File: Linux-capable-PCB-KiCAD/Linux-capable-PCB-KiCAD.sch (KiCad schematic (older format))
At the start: 36 parts, among them U1 A33

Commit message: Assigned footprints to components, antenna and a couple of other footprints need to be assigned
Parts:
- C1, C10, C11, C12, C13, C14, C15, C16, C17, C18, C19, C2, C20, C21, C22, C23, C24, C25, C3, C4, C5, C6, C7, C8, C9: footprint (none) -> Capacitor_SMD:C_0603_1608Metric
- MK1, MK2, MK3, MK4: footprint (none) -> MountingHole:MountingHole_3mm
- R1, R2, R3, R4, R5, R6: footprint (none) -> Resistor_SMD:R_0603_1608Metric
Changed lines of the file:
@@
 F 0 "R1" H 1920 2096 50  0000 L CNN
 F 1 "1k" H 1920 2005 50  0000 L CNN
-F 2 "" V 1780 2050 50  0001 C CNN
+F 2 "Resistor_SMD:R_0603_1608Metric" V 1780 2050 50  0001 C CNN
 F 3 "" H 1850 2050 50  0001 C CNN
 	1    1850 2050
@@
 F 0 "R2" H 1920 2496 50  0000 L CNN
 F 1 "1k" H 1920 2405 50  0000 L CNN
-F 2 "" V 1780 2450 50  0001 C CNN
+F 2 "Resistor_SMD:R_0603_1608Metric" V 1780 2450 50  0001 C CNN
 F 3 "" H 1850 2450 50  0001 C CNN
 	1    1850 2450
@@
 F 0 "C1" H 1515 2096 50  0000 L CNN
 F 1 "100n" H 1515 2005 50  0000 L CNN
-F 2 "" H 1438 1900 50  0001 C CNN
+F 2 "Capacitor_SMD:C_0603_1608Metric" H 1438 1900 50  0001 C CNN
 F 3 "" H 1400 2050 50  0001 C CNN
 	1    1400 2050
@@
 F 0 "C2" H 1515 2496 50  0000 L CNN
 F 1 "100n" H 1515 2405 50  0000 L CNN
-F 2 "" H 1438 2300 50  0001 C CNN
+F 2 "Capacitor_SMD:C_0603_1608Metric" H 1438 2300 50  0001 C CNN
 F 3 "" H 1400 2450 50  0001 C CNN
 	1    1400 2450
@@
 F 0 "C25" H 8565 4396 50  0000 L CNN
 F 1 "100n" H 8565 4305 50  0000 L CNN
-F 2 "" H 8488 4200 50  0001 C CNN
+F 2 "Capacitor_SMD:C_0603_1608Metric" H 8488 4200 50  0001 C CNN
 F 3 "" H 8450 4350 50  0001 C CNN
 	1    8450 4350
@@
 F 0 "R6" V 7093 2450 50  0000 C CNN
 F 1 "0R" V 7184 2450 50  0000 C CNN
-F 2 "" V 7230 2450 50  0001 C CNN
+F 2 "Resistor_SMD:R_0603_1608Metric" V 7230 2450 50  0001 C CNN
 F 3 "" H 7300 2450 50  0001 C CNN
 	1    7300 2450
@@
 F 0 "C17" H 7065 1846 50  0000 L CNN
 F 1 "10u" H 7065 1755 50  0000 L CNN
-F 2 "" H 6988 1650 50  0001 C CNN
+F 2 "Capacitor_SMD:C_0603_1608Metric" H 6988 1650 50  0001 C CNN
 F 3 "" H 6950 1800 50  0001 C CNN
 	1    6950 1800
@@
 F 0 "C22" H 7565 1846 50  0000 L CNN
 F 1 "100n" H 7565 1755 50  0000 L CNN
-F 2 "" H 7488 1650 50  0001 C CNN
+F 2 "Capacitor_SMD:C_0603_1608Metric" H 7488 1650 50  0001 C CNN
 F 3 "" H 7450 1800 50  0001 C CNN
 	1    7450 1800
@@
 F 0 "C13" H 6565 1846 50  0000 L CNN
 F 1 "22u" H 6500 1700 50  0000 L CNN
-F 2 "" H 6488 1650 50  0001 C CNN
+F 2 "Capacitor_SMD:C_0603_1608Metric" H 6488 1650 50  0001 C CNN
 F 3 "" H 6450 1800 50  0001 C CNN
 	1    6450 1800
@@
 F 0 "C9" H 6165 1846 50  0000 L CNN
 F 1 "100n" H 6100 1700 50  0000 L CNN
-F 2 "" H 6088 1650 50  0001 C CNN
+F 2 "Capacitor_SMD:C_0603_1608Metric" H 6088 1650 50  0001 C CNN
 F 3 "" H 6050 1800 50  0001 C CNN
 	1    6050 1800
@@
 F 0 "C5" H 5765 1846 50  0000 L CNN
 F 1 "100n" H 5700 1700 50  0000 L CNN
-F 2 "" H 5688 1650 50  0001 C CNN
+F 2 "Capacitor_SMD:C_0603_1608Metric" H 5688 1650 50  0001 C CNN
 F 3 "" H 5650 1800 50  0001 C CNN
 	1    5650 1800
@@
 F 0 "C3" H 5315 1846 50  0000 L CNN
 F 1 "100n" H 5250 1700 50  0000 L CNN
-F 2 "" H 5238 1650 50  0001 C CNN
+F 2 "Capacitor_SMD:C_0603_1608Metric" H 5238 1650 50  0001 C CNN
 F 3 "" H 5200 1800 50  0001 C CNN
 	1    5200 1800
@@
 F 0 "C6" H 5765 2846 50  0000 L CNN
 F 1 "100n" H 5700 2700 50  0000 L CNN
-F 2 "" H 5688 2650 50  0001 C CNN
+F 2 "Capacitor_SMD:C_0603_1608Metric" H 5688 2650 50  0001 C CNN
 F 3 "" H 5650 2800 50  0001 C CNN
 	1    5650 2800
@@
 F 0 "C10" H 6165 2846 50  0000 L CNN
 F 1 "100n" H 6100 2700 50  0000 L CNN
-F 2 "" H 6088 2650 50  0001 C CNN
+F 2 "Capacitor_SMD:C_0603_1608Metric" H 6088 2650 50  0001 C CNN
 F 3 "" H 6050 2800 50  0001 C CNN
 	1    6050 2800
@@
 F 0 "C14" H 6565 2846 50  0000 L CNN
 F 1 "100n" H 6500 2700 50  0000 L CNN
-F 2 "" H 6488 2650 50  0001 C CNN
+F 2 "Capacitor_SMD:C_0603_1608Metric" H 6488 2650 50  0001 C CNN
 F 3 "" H 6450 2800 50  0001 C CNN
 	1    6450 2800
@@
 F 0 "C7" H 5765 3946 50  0000 L CNN
 F 1 "22u" H 5700 3800 50  0000 L CNN
-F 2 "" H 5688 3750 50  0001 C CNN
+F 2 "Capacitor_SMD:C_0603_1608Metric" H 5688 3750 50  0001 C CNN
 F 3 "" H 5650 3900 50  0001 C CNN
 	1    5650 3900
@@
 F 0 "C11" H 6165 3946 50  0000 L CNN
 F 1 "100n" H 6100 3800 50  0000 L CNN
-F 2 "" H 6088 3750 50  0001 C CNN
+F 2 "Capacitor_SMD:C_0603_1608Metric" H 6088 3750 50  0001 C CNN
 F 3 "" H 6050 3900 50  0001 C CNN
 	1    6050 3900
@@
 F 0 "C15" H 6665 3946 50  0000 L CNN
 F 1 "100n" H 6600 3800 50  0000 L CNN
-F 2 "" H 6588 3750 50  0001 C CNN
+F 2 "Capacitor_SMD:C_0603_1608Metric" H 6588 3750 50  0001 C CNN
 F 3 "" H 6550 3900 50  0001 C CNN
 	1    6550 3900
@@
 F 0 "C18" H 7065 3946 50  0000 L CNN
 F 1 "100n" H 7000 3800 50  0000 L CNN
-F 2 "" H 6988 3750 50  0001 C CNN
+F 2 "Capacitor_SMD:C_0603_1608Metric" H 6988 3750 50  0001 C CNN
 F 3 "" H 6950 3900 50  0001 C CNN
 	1    6950 3900
@@
 F 0 "C20" H 7465 3946 50  0000 L CNN
 F 1 "100n" H 7400 3800 50  0000 L CNN
-F 2 "" H 7388 3750 50  0001 C CNN
+F 2 "Capacitor_SMD:C_0603_1608Metric" H 7388 3750 50  0001 C CNN
 F 3 "" H 7350 3900 50  0001 C CNN
 	1    7350 3900
@@
 F 0 "C23" H 7815 3946 50  0000 L CNN
 F 1 "22u" H 7750 3800 50  0000 L CNN
-F 2 "" H 7738 3750 50  0001 C CNN
+F 2 "Capacitor_SMD:C_0603_1608Metric" H 7738 3750 50  0001 C CNN
 F 3 "" H 7700 3900 50  0001 C CNN
 	1    7700 3900
@@
 F 0 "C4" H 5365 4946 50  0000 L CNN
 F 1 "100n" H 5300 4800 50  0000 L CNN
-F 2 "" H 5288 4750 50  0001 C CNN
+F 2 "Capacitor_SMD:C_0603_1608Metric" H 5288 4750 50  0001 C CNN
 F 3 "" H 5250 4900 50  0001 C CNN
 	1    5250 4900
@@
 F 0 "C8" H 5765 4946 50  0000 L CNN
 F 1 "100n" H 5700 4800 50  0000 L CNN
-F 2 "" H 5688 4750 50  0001 C CNN
+F 2 "Capacitor_SMD:C_0603_1608Metric" H 5688 4750 50  0001 C CNN
 F 3 "" H 5650 4900 50  0001 C CNN
 	1    5650 4900
@@
 F 0 "C12" H 6165 4946 50  0000 L CNN
 F 1 "22u" H 6100 4800 50  0000 L CNN
-F 2 "" H 6088 4750 50  0001 C CNN
+F 2 "Capacitor_SMD:C_0603_1608Metric" H 6088 4750 50  0001 C CNN
 F 3 "" H 6050 4900 50  0001 C CNN
 	1    6050 4900
@@
 F 0 "C16" H 6665 4996 50  0000 L CNN
 F 1 "100n" H 6600 4850 50  0000 L CNN
-F 2 "" H 6588 4800 50  0001 C CNN
+F 2 "Capacitor_SMD:C_0603_1608Metric" H 6588 4800 50  0001 C CNN
 F 3 "" H 6550 4950 50  0001 C CNN
 	1    6550 4950
@@
 F 0 "C19" H 7065 4996 50  0000 L CNN
 F 1 "100n" H 7000 4850 50  0000 L CNN
-F 2 "" H 6988 4800 50  0001 C CNN
+F 2 "Capacitor_SMD:C_0603_1608Metric" H 6988 4800 50  0001 C CNN
 F 3 "" H 6950 4950 50  0001 C CNN
 	1    6950 4950
@@
 F 0 "C21" H 7465 4996 50  0000 L CNN
 F 1 "100n" H 7400 4850 50  0000 L CNN
-F 2 "" H 7388 4800 50  0001 C CNN
+F 2 "Capacitor_SMD:C_0603_1608Metric" H 7388 4800 50  0001 C CNN
 F 3 "" H 7350 4950 50  0001 C CNN
 	1    7350 4950
@@
 F 0 "C24" H 7815 4996 50  0000 L CNN
 F 1 "22u" H 7750 4850 50  0000 L CNN
-F 2 "" H 7738 4800 50  0001 C CNN
+F 2 "Capacitor_SMD:C_0603_1608Metric" H 7738 4800 50  0001 C CNN
 F 3 "" H 7700 4950 50  0001 C CNN
 	1    7700 4950
@@
 F 0 "R5" V 2200 5400 50  0000 C CNN
 F 1 "240R" V 2350 5550 50  0000 C CNN
-F 2 "" V 2180 5550 50  0001 C CNN
+F 2 "Resistor_SMD:R_0603_1608Metric" V 2180 5550 50  0001 C CNN
 F 3 "" H 2250 5550 50  0001 C CNN
 	1    2250 5550
@@
 F 0 "R4" V 2200 4900 50  0000 C CNN
 F 1 "22R" V 2250 5050 50  0000 C CNN
-F 2 "" V 2180 5050 50  0001 C CNN
+F 2 "Resistor_SMD:R_0603_1608Metric" V 2180 5050 50  0001 C CNN
 F 3 "" H 2250 5050 50  0001 C CNN
 	1    2250 5050
@@
 F 0 "R3" V 2200 4800 50  0000 C CNN
 F 1 "22R" V 2250 4950 50  0000 C CNN
-F 2 "" V 2180 4950 50  0001 C CNN
+F 2 "Resistor_SMD:R_0603_1608Metric" V 2180 4950 50  0001 C CNN
 F 3 "" H 2250 4950 50  0001 C CNN
 	1    2250 4950
@@
 F 0 "MK1" H 4200 946 50  0000 L CNN
 F 1 "Mounting_Hole" H 4200 855 50  0000 L CNN
-F 2 "" H 4100 900 50  0001 C CNN
+F 2 "MountingHole:MountingHole_3mm" H 4100 900 50  0001 C CNN
 F 3 "" H 4100 900 50  0001 C CNN
 	1    4100 900
@@
 F 0 "MK2" H 4200 1246 50  0000 L CNN
 F 1 "Mounting_Hole" H 4200 1155 50  0000 L CNN
-F 2 "" H 4100 1200 50  0001 C CNN
+F 2 "MountingHole:MountingHole_3mm" H 4100 1200 50  0001 C CNN
 F 3 "" H 4100 1200 50  0001 C CNN
 	1    4100 1200
@@
 F 0 "MK3" H 4200 1546 50  0000 L CNN
 F 1 "Mounting_Hole" H 4200 1455 50  0000 L CNN
-F 2 "" H 4100 1500 50  0001 C CNN
+F 2 "MountingHole:MountingHole_3mm" H 4100 1500 50  0001 C CNN
 F 3 "" H 4100 1500 50  0001 C CNN
 	1    4100 1500
@@
 F 0 "MK4" H 4200 1846 50  0000 L CNN
 F 1 "Mounting_Hole" H 4200 1755 50  0000 L CNN
-F 2 "" H 4100 1800 50  0001 C CNN
+F 2 "MountingHole:MountingHole_3mm" H 4100 1800 50  0001 C CNN
 F 3 "" H 4100 1800 50  0001 C CNN
 	1    4100 1800

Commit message: CPU and RAM
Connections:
- net labels added: DCK_N, DCK_P
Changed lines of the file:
@@
 F4 "~CS" I L 1750 7000 50
 F5 "~CKE" I L 1750 6500 50
-F6 "CK" I L 1750 6750 50
-F7 "~CK" I L 1750 6625 50
+F6 "CK_P" I L 1750 6750 50
+F7 "CK_N" I L 1750 6625 50
 F8 "~RAS" I L 1750 7125 50
 F9 "~CAS" I L 1750 7250 50
@@
 Wire Bus Line
 	3925 2350 3925 3850
+Text Label 2425 4950 1    50   ~ 0
+DCK_P
+Text Label 2425 5050 3    50   ~ 0
+DCK_N
 $EndSCHEMATC

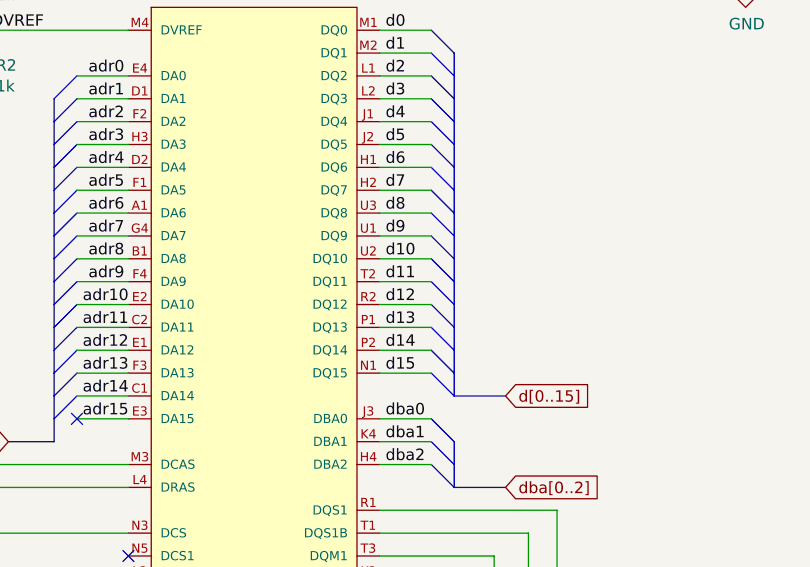
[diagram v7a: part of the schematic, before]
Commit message: DDR3 - CPU layout
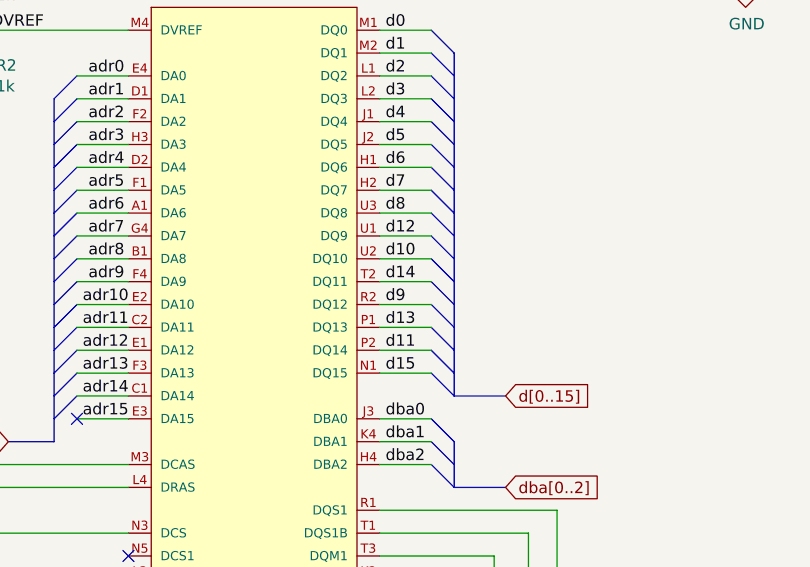
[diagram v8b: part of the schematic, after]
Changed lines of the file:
@@
 Text Label 3625 3050 0    50   ~ 0
 d8
-Text Label 3625 3150 0    50   ~ 0
+Text Label 3625 3450 0    50   ~ 0
 d9
 Text Label 3625 3250 0    50   ~ 0
 d10
+Text Label 3625 3650 0    50   ~ 0
+d11
+Text Label 3625 3150 0    50   ~ 0
+d12
 Text Label 3625 3350 0    50   ~ 0
-d11
-Text Label 3625 3450 0    50   ~ 0
-d12
-Text Label 3625 3550 0    50   ~ 0
-d13
-Text Label 3625 3650 0    50   ~ 0
 d14
-Text Label 3625 3750 0    50   ~ 0
-d15
 Text Label 3625 3950 0    50   ~ 0
 dba0
@@
 Text Label 2425 5050 3    50   ~ 0
 DCK_N
+Text Label 3625 3750 0    50   ~ 0
+d15
+Text Label 3625 3550 0    50   ~ 0
+d13
 $EndSCHEMATC
